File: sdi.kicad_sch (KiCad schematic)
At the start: 78 parts, among them J2 031-70526-21, J3 031-70526-21, U11 LIFCL-40-9BG256C, U15 GS2971A, U16 GS2988, Y1 ABM7_27.000MH_D2Y_T

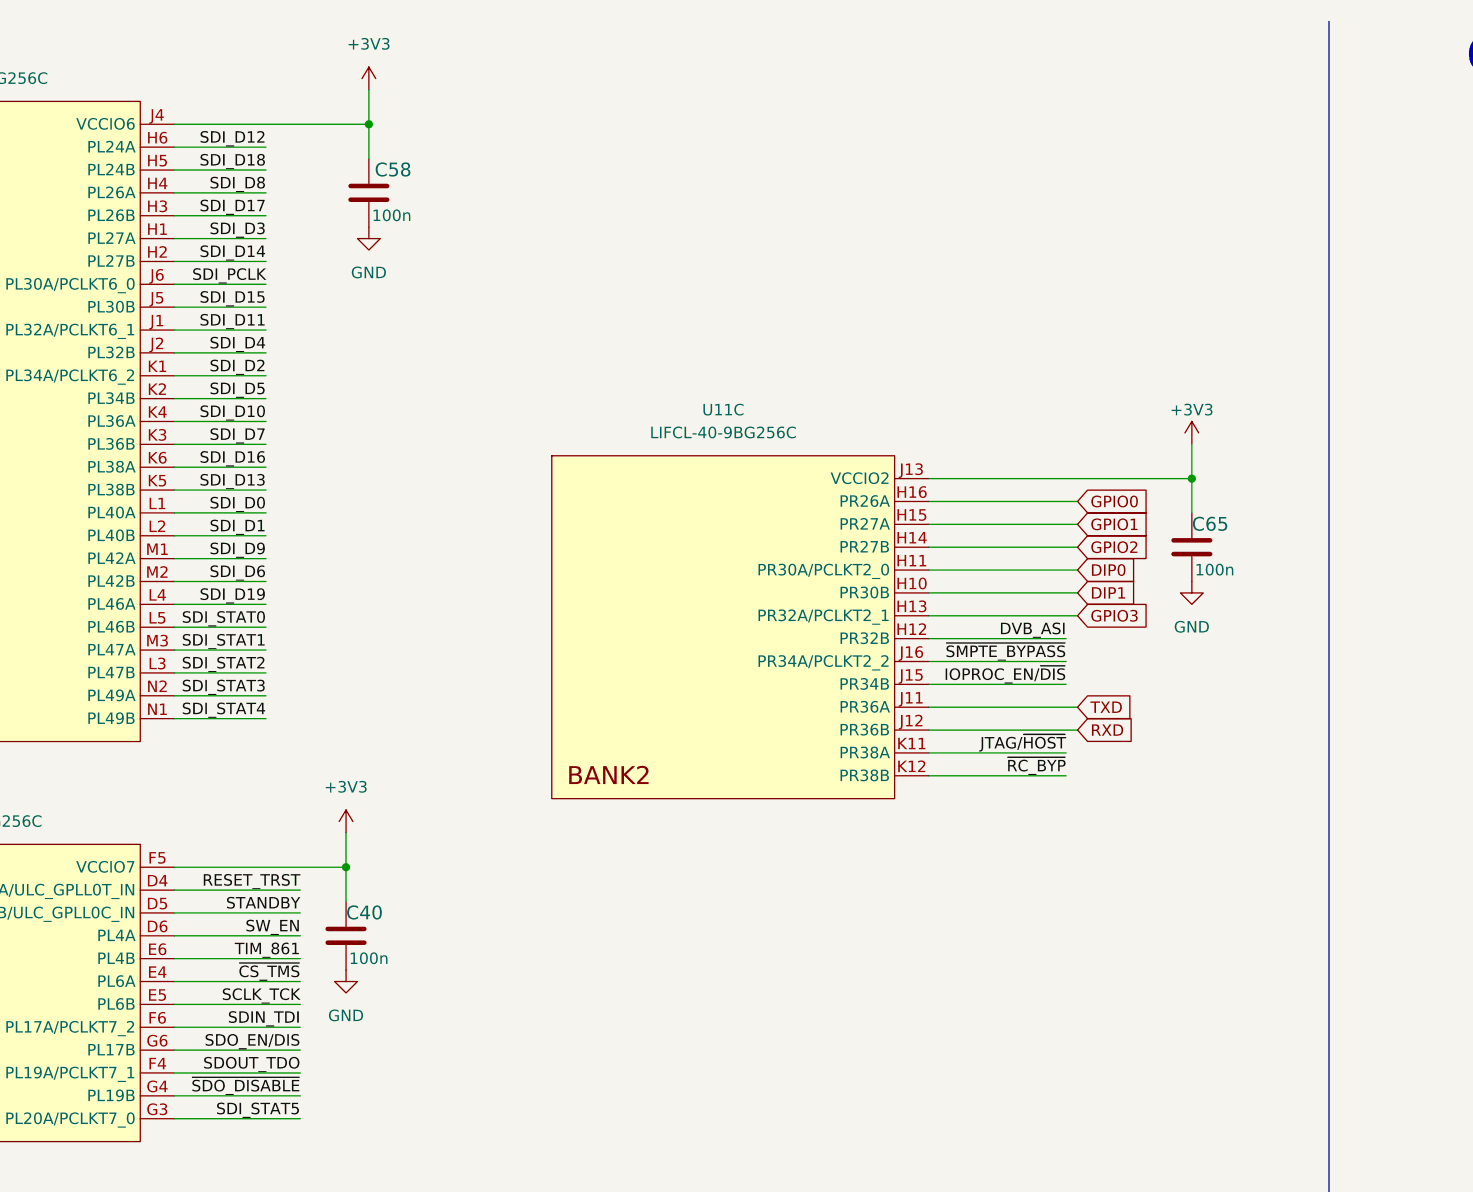
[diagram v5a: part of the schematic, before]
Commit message: Update PCB routing
- apply new DRC
- add FPGA package delay to the high speed traces tunning
- improve GND and power planes
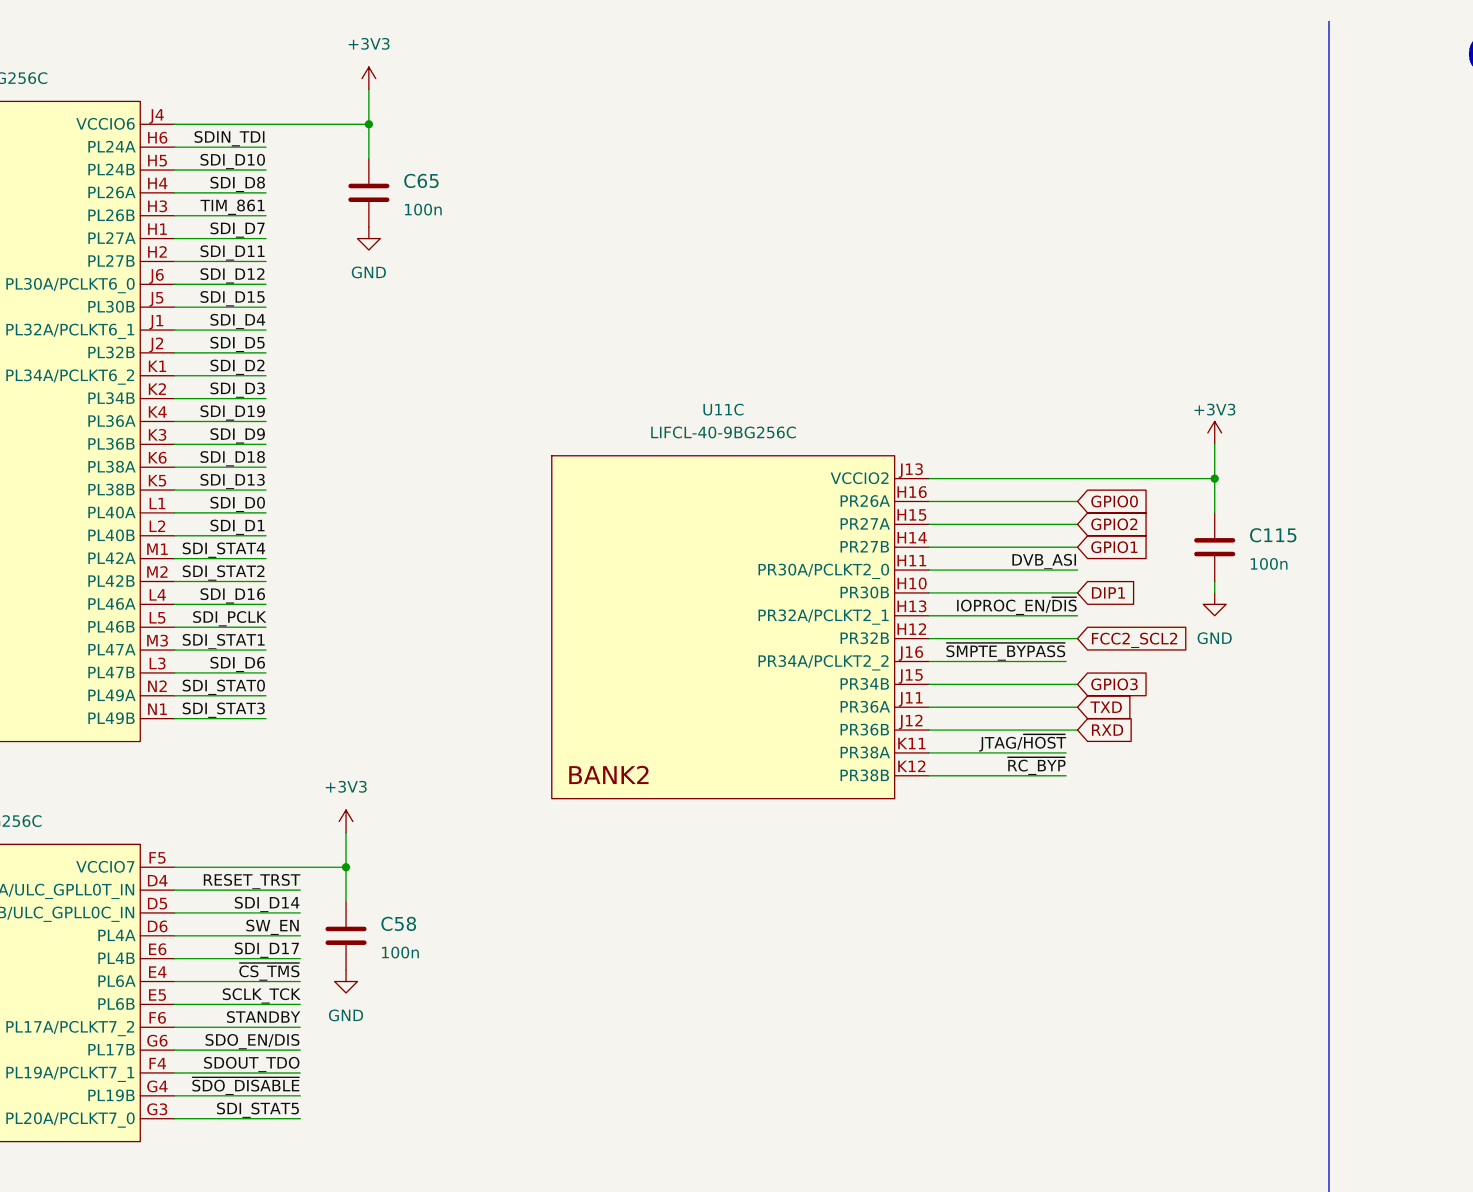
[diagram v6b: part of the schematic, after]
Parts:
- removed C40, C58, C65: C_100n_0402, crosslink-nx-video-converter-footprints:0402-cap, symbol crosslink-nx-video-converter:C_100n_0402
- added C115, C58, C65: C_100n_0201, crosslink-nx-video-converter-footprints:0201-res, symbol crosslink-nx-video-converter:C_100n_0201
- U11: footprint crosslink-nx-video-converter-footprints:BGA-256_16x16_14.0x14.0mm -> crosslink-nx-video-converter-footprints:CrosslinkNX-BGA-256_16x16_14.0x14.0mm
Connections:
- net DIP0 is gone; now on net DVB_ASI: U11.H11 (PR30A/PCLKT2_0)
- net +3V3: now also C115.1, C58.1, C65.1
- net DVB_ASI: no longer U11.H12 (PR32B)
- net GND: now also C115.2, C58.2, C65.2
- net GPIO1: now also U11.H14 (PR27B); no longer U11.H15 (PR27A)
- net GPIO2: now also U11.H15 (PR27A); no longer U11.H14 (PR27B)
- net GPIO3: now also U11.J15 (PR34B); no longer U11.H13 (PR32A/PCLKT2_1)
- net IOPROC_EN/~{DIS}: now also U11.H13 (PR32A/PCLKT2_1); no longer U11.J15 (PR34B)
- net SDIN_TDI: now also U11.H6 (PL24A); no longer U11.F6 (PL17A/PCLKT7_2)
- net SDI_D10: now also U11.H5 (PL24B); no longer U11.K4 (PL36A)
- net SDI_D11: now also U11.H2 (PL27B); no longer U11.J1 (PL32A/PCLKT6_1)
- net SDI_D12: now also U11.J6 (PL30A/PCLKT6_0); no longer U11.H6 (PL24A)
- net SDI_D14: now also U11.D5 (PL3B/ULC_GPLL0C_IN); no longer U11.H2 (PL27B)
- net SDI_D16: now also U11.L4 (PL46A); no longer U11.K6 (PL38A)
- net SDI_D17: now also U11.E6 (PL4B); no longer U11.H3 (PL26B)
- net SDI_D18: now also U11.K6 (PL38A); no longer U11.H5 (PL24B)
- net SDI_D19: now also U11.K4 (PL36A); no longer U11.L4 (PL46A)
- net SDI_D3: now also U11.K2 (PL34B); no longer U11.H1 (PL27A)
- net SDI_D4: now also U11.J1 (PL32A/PCLKT6_1); no longer U11.J2 (PL32B)
- net SDI_D5: now also U11.J2 (PL32B); no longer U11.K2 (PL34B)
- net SDI_D6: now also U11.L3 (PL47B); no longer U11.M2 (PL42B)
- net SDI_D7: now also U11.H1 (PL27A); no longer U11.K3 (PL36B)
- net SDI_D9: now also U11.K3 (PL36B); no longer U11.M1 (PL42A)
- net SDI_PCLK: now also U11.L5 (PL46B); no longer U11.J6 (PL30A/PCLKT6_0)
- net SDI_STAT0: now also U11.N2 (PL49A); no longer U11.L5 (PL46B)
- net SDI_STAT2: now also U11.M2 (PL42B); no longer U11.L3 (PL47B)
- net SDI_STAT3: now also U11.N1 (PL49B); no longer U11.N2 (PL49A)
- net SDI_STAT4: now also U11.M1 (PL42A); no longer U11.N1 (PL49B)
- net STANDBY: now also U11.F6 (PL17A/PCLKT7_2); no longer U11.D5 (PL3B/ULC_GPLL0C_IN)
- net TIM_861: now also U11.H3 (PL26B); no longer U11.E6 (PL4B)
- new net FCC2_SCL2: U11.H12 (PR32B)

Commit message: Update project naming convention
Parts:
- C115, C58, C65: footprint crosslink-nx-video-converter-footprints:0201-res -> sdi-mipi-cross-converter-footprints:0201-res; symbol crosslink-nx-video-converter:C_100n_0201 -> sdi-mipi-cross-converter:C_100n_0201
- C51, C52: footprint crosslink-nx-video-converter-footprints:0402-cap -> sdi-mipi-cross-converter-footprints:0402-cap; symbol crosslink-nx-video-converter:C_33p_0402 -> sdi-mipi-cross-converter:C_33p_0402
- C53, C54, C57: footprint crosslink-nx-video-converter-footprints:0402-cap -> sdi-mipi-cross-converter-footprints:0402-cap; symbol crosslink-nx-video-converter:C_1u_0402 -> sdi-mipi-cross-converter:C_1u_0402
- C55: footprint crosslink-nx-video-converter-footprints:0402-cap -> sdi-mipi-cross-converter-footprints:0402-cap; symbol crosslink-nx-video-converter:C_47n_0402 -> sdi-mipi-cross-converter:C_47n_0402
- C56, C59: footprint crosslink-nx-video-converter-footprints:0402-cap -> sdi-mipi-cross-converter-footprints:0402-cap; symbol crosslink-nx-video-converter:C_470n_0402 -> sdi-mipi-cross-converter:C_470n_0402
- C60, C61, C62, C63, C64, C66, C67, C68, C69, C70, C72, C73, C74: footprint crosslink-nx-video-converter-footprints:0402-cap -> sdi-mipi-cross-converter-footprints:0402-cap; symbol crosslink-nx-video-converter:C_100n_0402 -> sdi-mipi-cross-converter:C_100n_0402
- C71: footprint crosslink-nx-video-converter-footprints:0603-cap -> sdi-mipi-cross-converter-footprints:0603-cap; symbol crosslink-nx-video-converter:C_33u_0603 -> sdi-mipi-cross-converter:C_33u_0603
- C76: footprint crosslink-nx-video-converter-footprints:0402-cap -> sdi-mipi-cross-converter-footprints:0402-cap; symbol crosslink-nx-video-converter:C_10n_0402 -> sdi-mipi-cross-converter:C_10n_0402
- C77, C78: footprint crosslink-nx-video-converter-footprints:0402-cap -> sdi-mipi-cross-converter-footprints:0402-cap; symbol crosslink-nx-video-converter:C_4u7_0402 -> sdi-mipi-cross-converter:C_4u7_0402
- D7, D8: footprint crosslink-nx-video-converter-footprints:LED_0603 -> sdi-mipi-cross-converter-footprints:LED_0603; symbol crosslink-nx-video-converter:LTST-C190GKT -> sdi-mipi-cross-converter:LTST-C190GKT
- J2, J3: footprint crosslink-nx-video-converter-footprints:BNC_Edge_Conn -> sdi-mipi-cross-converter-footprints:BNC_Edge_Conn; symbol crosslink-nx-video-converter:031-70526-21 -> sdi-mipi-cross-converter:031-70526-21
- L4, L5: footprint crosslink-nx-video-converter-footprints:0402-cap -> sdi-mipi-cross-converter-footprints:0402-cap; symbol crosslink-nx-video-converter:L_0402_6n2 -> sdi-mipi-cross-converter:L_0402_6n2
- R100, R101: footprint crosslink-nx-video-converter-footprints:0603-res -> sdi-mipi-cross-converter-footprints:0603-res; symbol crosslink-nx-video-converter:R_200R_0603 -> sdi-mipi-cross-converter:R_200R_0603
- R137, R138, R139, R140: footprint crosslink-nx-video-converter-footprints:0402-res -> sdi-mipi-cross-converter-footprints:0402-res; symbol crosslink-nx-video-converter:R_1k_0402 -> sdi-mipi-cross-converter:R_1k_0402
- R38: footprint crosslink-nx-video-converter-footprints:0402-res -> sdi-mipi-cross-converter-footprints:0402-res; symbol crosslink-nx-video-converter:R_0R_0402 -> sdi-mipi-cross-converter:R_0R_0402
- R51, R52, R59, R60, R61, R62: footprint crosslink-nx-video-converter-footprints:0402-res -> sdi-mipi-cross-converter-footprints:0402-res; symbol crosslink-nx-video-converter:R_75R_0402 -> sdi-mipi-cross-converter:R_75R_0402
- R53: footprint crosslink-nx-video-converter-footprints:0402-res -> sdi-mipi-cross-converter-footprints:0402-res; symbol crosslink-nx-video-converter:R_37R4_0402 -> sdi-mipi-cross-converter:R_37R4_0402
- R54, R55: footprint crosslink-nx-video-converter-footprints:0402-res -> sdi-mipi-cross-converter-footprints:0402-res; symbol crosslink-nx-video-converter:R_100k_0402 -> sdi-mipi-cross-converter:R_100k_0402
- R56: footprint crosslink-nx-video-converter-footprints:0402-res -> sdi-mipi-cross-converter-footprints:0402-res; symbol crosslink-nx-video-converter:R_105R_0402 -> sdi-mipi-cross-converter:R_105R_0402
- R57: footprint crosslink-nx-video-converter-footprints:0402-res -> sdi-mipi-cross-converter-footprints:0402-res; symbol crosslink-nx-video-converter:R_750R_0402 -> sdi-mipi-cross-converter:R_750R_0402
- TP13, TP14, TP24, TP25, TP26, TP27, TP28, TP29, TP30, TP31, TP32, TP33, TP34, TP35, TP36, TP37, TP38, TP39, TP40, TP41, TP42, TP43: footprint crosslink-nx-video-converter-footprints:Testpoint_smd_0_75mm -> sdi-mipi-cross-converter-footprints:Testpoint_smd_0_75mm; symbol crosslink-nx-video-converter:TP_SMD_0_75MM -> sdi-mipi-cross-converter:TP_SMD_0_75MM
- U11: footprint crosslink-nx-video-converter-footprints:CrosslinkNX-BGA-256_16x16_14.0x14.0mm -> sdi-mipi-cross-converter-footprints:CrosslinkNX-BGA-256_16x16_14.0x14.0mm; symbol crosslink-nx-video-converter:LIFCL-40-9BG256C -> sdi-mipi-cross-converter:LIFCL-40-9BG256C
- U15: footprint crosslink-nx-video-converter-footprints:BGA100_11x11mm -> sdi-mipi-cross-converter-footprints:BGA100_11x11mm; symbol crosslink-nx-video-converter:GS2971A -> sdi-mipi-cross-converter:GS2971A
- U16: footprint crosslink-nx-video-converter-footprints:QFN-16_EP_4x4_Pitch0.65mm -> sdi-mipi-cross-converter-footprints:QFN-16_EP_4x4_Pitch0.65mm; symbol crosslink-nx-video-converter:GS2988 -> sdi-mipi-cross-converter:GS2988
- Y1: footprint crosslink-nx-video-converter-footprints:ABM7_OSC -> sdi-mipi-cross-converter-footprints:ABM7_OSC; symbol crosslink-nx-video-converter:ABM7_27.000MH_D2Y_T -> sdi-mipi-cross-converter:ABM7_27.000MH_D2Y_T

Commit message: Bump to 1.1.0, update naming
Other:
- title: CrossLink-NX Video Converter -> SDI-MIPI Cross Converter
